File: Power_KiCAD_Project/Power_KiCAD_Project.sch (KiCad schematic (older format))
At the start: 5 parts

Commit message: Changed labels from global to local
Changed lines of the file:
@@
 Text Notes 1750 2900 2    100  ~ 0
 SWD Connector
-Text GLabel 1300 1500 2    50   Input ~ 0
-I2C1_SDA
-Text GLabel 1300 1600 2    50   Input ~ 0
-I2C1_SCL
 Text Notes 600  2400 0    50   ~ 0
 Current version uses connector data\nbus for communications to BMS.\nThis may not be ideal, and perhaps a \ndedicated communcation line\nto the BMS should be used instead.
@@
 Wire Bus Line
 	5600 1050 5600 2600
+Text Label 1300 1500 0    50   ~ 0
+I2C1_SDA
+Text Label 1300 1600 0    50   ~ 0
+I2C1_SCL
 $EndSCHEMATC

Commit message: Updated With c=Connections
Added connections for power and for card slots
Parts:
- added J?: Barrel_Jack, symbol Connector:Barrel_Jack
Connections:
- wire segments 75 -> 79
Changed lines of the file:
@@
 $Descr A4 11693 8268
 encoding utf-8
-Sheet 1 5
+Sheet 1 6
 Title "Power Supply PCB Schematic"
 Date "2021-10-05"
@@
 	2500 5450 2500 5300
 Wire Wire Line
-	2500 5300 3100 5300
+	2500 5300 2950 5300
 Wire Wire Line
 	1500 5550 2500 5550
@@
 	2500 5550 2500 6050
 Wire Wire Line
-	2500 6050 3100 6050
+	2500 6050 2750 6050
 Wire Wire Line
 	1400 3350 2150 3350
@@
 NoConn ~ 1300 1700
 NoConn ~ 1300 1800
+Text Label 1300 1500 0    50   ~ 0
+I2C1_SDA
+Text Label 1300 1600 0    50   ~ 0
+I2C1_SCL
+$Sheet
+S 8500 4550 2050 1400
+U 6183A598
+F0 "Pcie_Connection" 50
+F1 "Pcie_Connection.sch" 50
+$EndSheet
+$Comp
+L Connector:Barrel_Jack J?
+U 1 1 61850F95
+P 2850 4550
+F 0 "J?" V 2861 4738 50  0000 L CNN
+F 1 "Barrel_Jack" V 2952 4738 50  0000 L CNN
+F 2 "" H 2900 4510 50  0001 C CNN
+F 3 "~" H 2900 4510 50  0001 C CNN
+	1    2850 4550
+	0    1    1    0
+$EndComp
+Wire Wire Line
+	2950 4850 2950 5300
+Connection ~ 2950 5300
+Wire Wire Line
+	2950 5300 3100 5300
+Wire Wire Line
+	2750 4850 2750 6050
 Wire Bus Line
 	1350 6500 1350 6800
@@
 Wire Bus Line
 	5600 1050 5600 2600
-Text Label 1300 1500 0    50   ~ 0
-I2C1_SDA
-Text Label 1300 1600 0    50   ~ 0
-I2C1_SCL
+Connection ~ 2750 6050
+Wire Wire Line
+	2750 6050 3100 6050
 $EndSCHEMATC

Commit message: Changes to bus
bus was changed
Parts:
- removed C?: 100nF, symbol Device:C_Small
- removed J?: ARM 10 Pin, 2X5-RA, symbol SparkFun-Connectors:CONN_05X2RA
- removed J?: CONN_06X2SMD_FEMALE, 2X6_SMD, symbol SparkFun-Connectors:CONN_06X2SMD_FEMALE
- removed J?: CONN_03X2FEMALE, 2X3, symbol SparkFun-Connectors:CONN_03X2FEMALE
- added J1, J3, J4, J5: XT60, 1X02, symbol SparkFun-Connectors:CONN_02
- J2: renamed from J?; Field4 LiPo Pack Connector -> Pack 2
- gave numbers to parts that had none: 1
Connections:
- net labels added: Alert_active, Alert_scl, Alert_sda, NRST, SWCLK, SWDIO
- net labels removed: +5V, I2C1_SCL, I2C1_SDA
- wire segments 79 -> 32
- no-connect marks 11 -> 24
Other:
- note removed: "Current version uses connector data\nbus for communications to BMS.\nThis may not be ideal, and perhaps a \ndedicated communcation line\nto the BMS should be used instead."
- note removed: "Main System Bus"
- note removed: "NRST cap protects\nagainst parasitic resets."
- note removed: "SWD Connector"
- moved on the sheet: J2

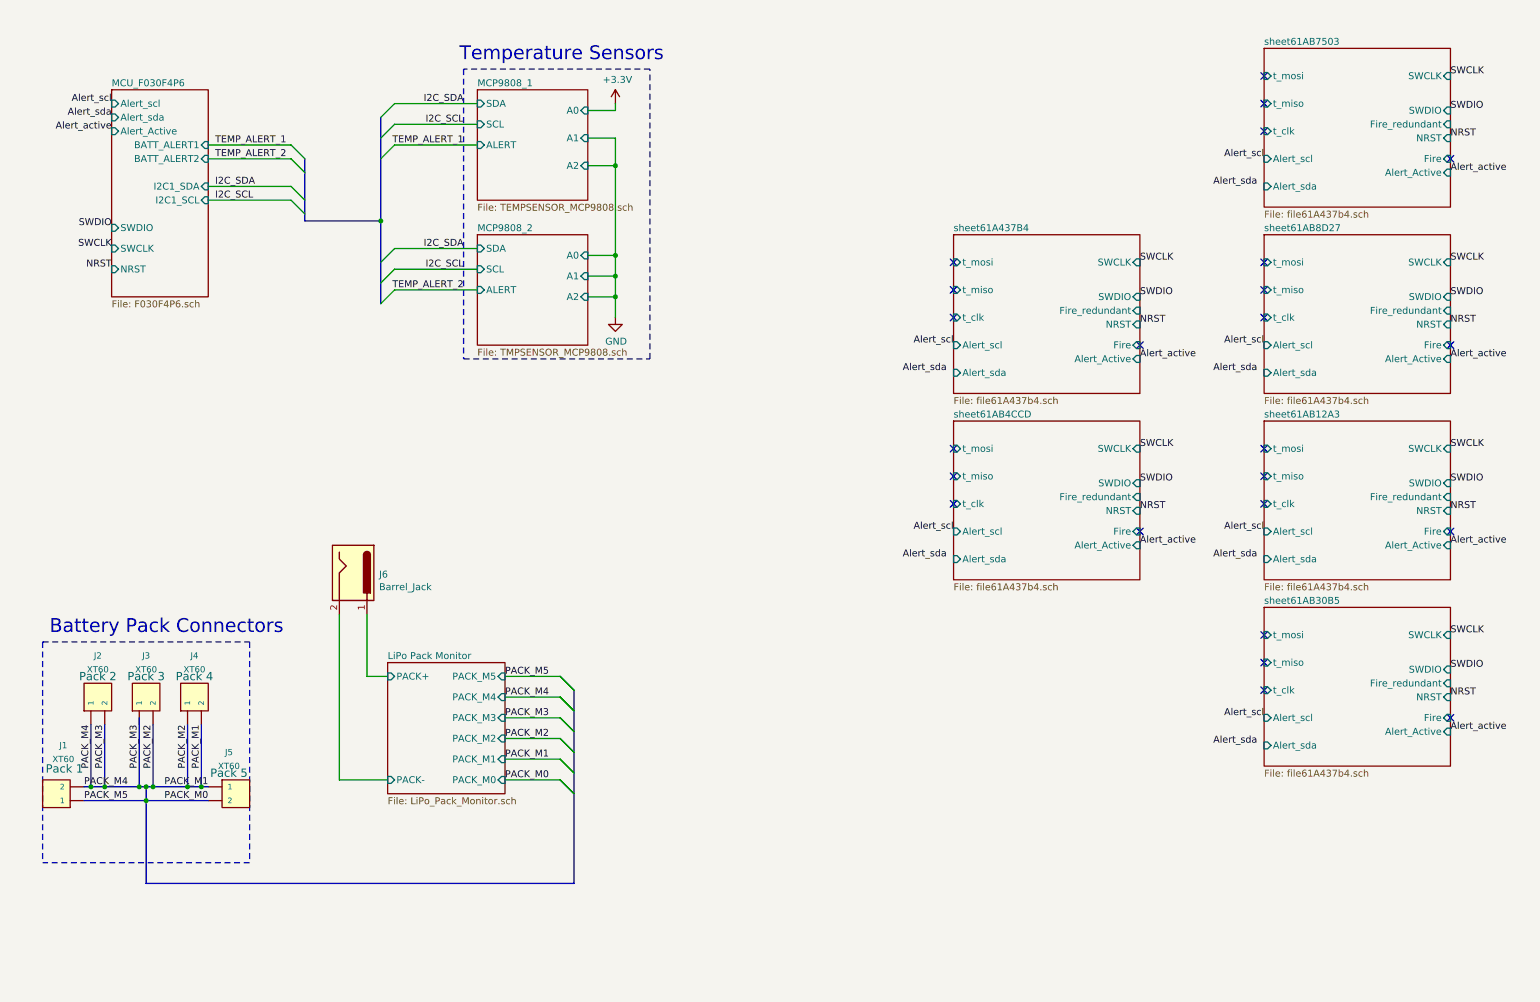
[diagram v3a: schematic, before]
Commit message: Added main Buck Converters & Question about grounding
I think that the BMS Ground needs to be separated from the main board ground since the BMS uses low side switching to protect the batteries. Like it is currently setup, the current can bypass the switches through ground.
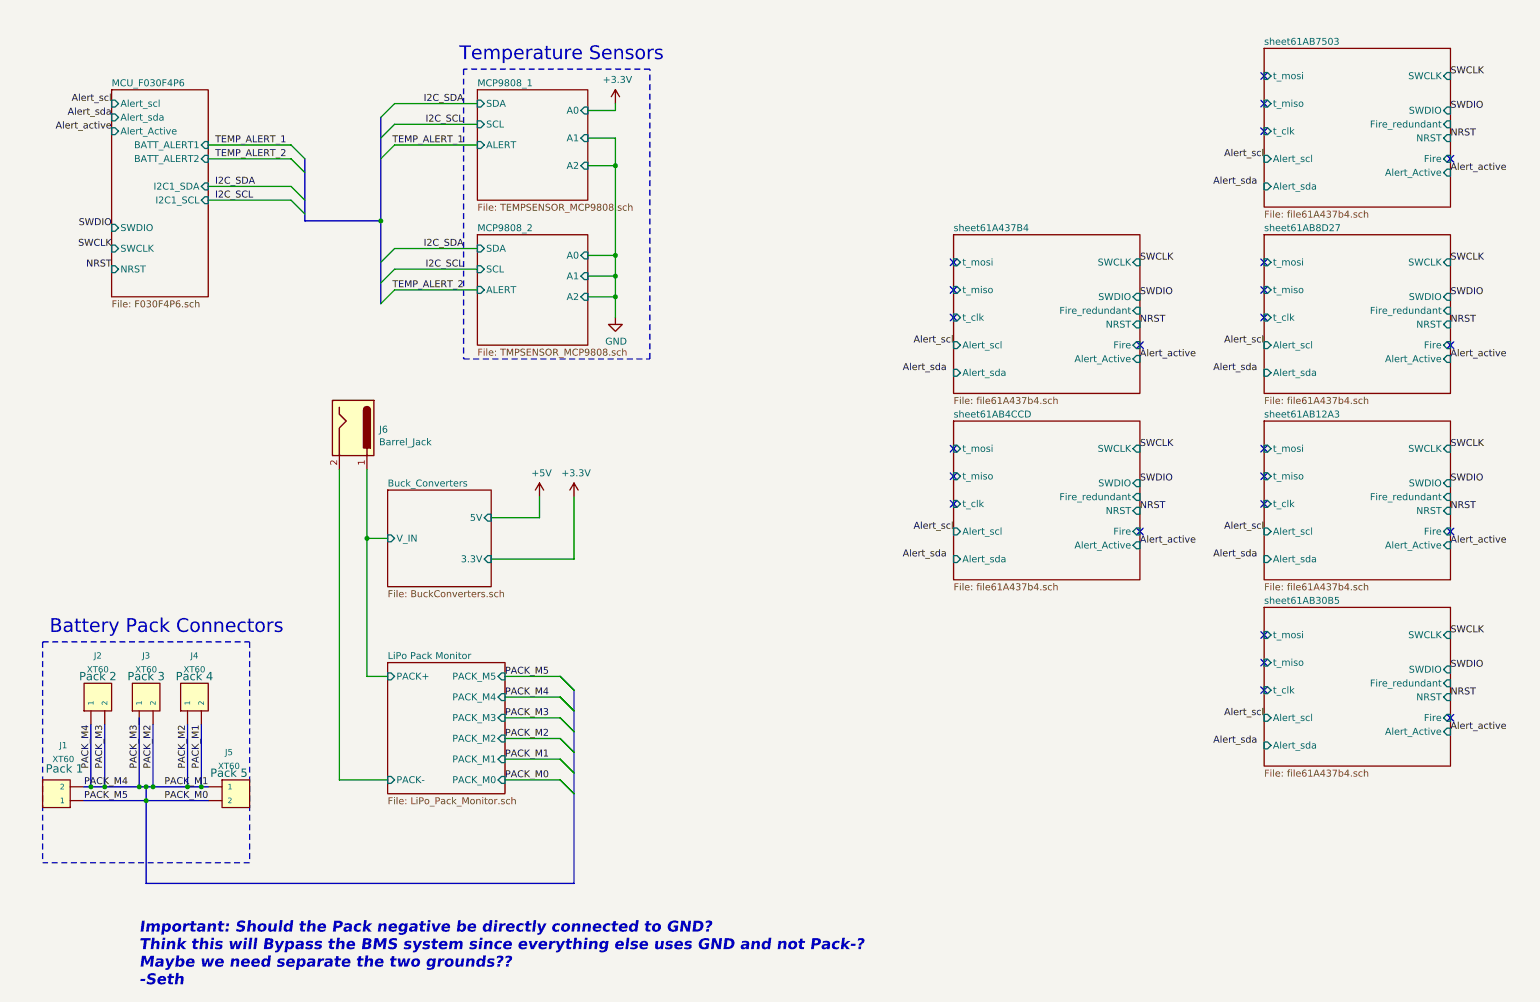
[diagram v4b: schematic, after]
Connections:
- net LiPo Pack Monitor/PACK+ renamed Buck_Converters/V_IN
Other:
- note added: "Important: Should the Pack negative be directly connected to GND?\nThink this will Bypass the BMS system since everything else uses GND and not Pack-?\nMaybe we need separate the two grounds??\n-Seth"
- moved on the sheet: J6
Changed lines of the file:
@@
 $Descr A4 11693 8268
 encoding utf-8
-Sheet 1 11
+Sheet 1 12
 Title "Power Supply PCB Schematic"
 Date "2021-10-05"
@@
 L Connector:Barrel_Jack J6
 U 1 1 61850F95
-P 2850 4550
-F 0 "J6" V 2861 4738 50  0000 L CNN
-F 1 "Barrel_Jack" V 2952 4738 50  0000 L CNN
-F 2 "" H 2900 4510 50  0001 C CNN
-F 3 "~" H 2900 4510 50  0001 C CNN
-	1    2850 4550
+P 2850 3500
+F 0 "J6" V 2861 3688 50  0000 L CNN
+F 1 "Barrel_Jack" V 2952 3688 50  0000 L CNN
+F 2 "" H 2900 3460 50  0001 C CNN
+F 3 "~" H 2900 3460 50  0001 C CNN
+	1    2850 3500
 	0    1    1    0
 $EndComp
 Wire Wire Line
-	2950 4850 2950 5300
-Wire Wire Line
 	2950 5300 3100 5300
-Wire Wire Line
-	2750 4850 2750 6050
 Wire Wire Line
 	2750 6050 3100 6050
@@
 Wire Bus Line
 	1050 5650 1050 6100
-Wire Bus Line
-	3050 2000 3050 2600
-Wire Bus Line
-	3050 1250 3050 2000
-Wire Bus Line
-	2500 1550 2500 2000
-Wire Bus Line
-	4450 5400 4450 6800
 Connection ~ 1050 6100
 Wire Bus Line
@@
 Text Label 1800 6200 2    50   ~ 0
 PACK_M0
+$Sheet
+S 3100 3950 750  700
+U 61A48488
+F0 "Buck_Converters" 50
+F1 "BuckConverters.sch" 50
+F2 "V_IN" I L 3100 4300 50
+F3 "3.3V" I R 3850 4450 50
+F4 "5V" I R 3850 4150 50
+$EndSheet
+Wire Wire Line
+	2750 3800 2750 6050
+Wire Wire Line
+	2950 3800 2950 4300
+Wire Wire Line
+	3100 4300 2950 4300
+Connection ~ 2950 4300
+Wire Wire Line
+	2950 4300 2950 5300
+$Comp
+L power:+3.3V #PWR?
+U 1 1 61A5452E
+P 4450 4000
+F 0 "#PWR?" H 4450 3850 50  0001 C CNN
+F 1 "+3.3V" H 4465 4173 50  0000 C CNN
+F 2 "" H 4450 4000 50  0001 C CNN
+F 3 "" H 4450 4000 50  0001 C CNN
+	1    4450 4000
+	1    0    0    -1
+$EndComp
+$Comp
+L power:+5V #PWR?
+U 1 1 61A56282
+P 4200 4000
+F 0 "#PWR?" H 4200 3850 50  0001 C CNN
+F 1 "+5V" H 4215 4173 50  0000 C CNN
+F 2 "" H 4200 4000 50  0001 C CNN
+F 3 "" H 4200 4000 50  0001 C CNN
+	1    4200 4000
+	1    0    0    -1
+$EndComp
+Wire Wire Line
+	3850 4150 4200 4150
+Wire Wire Line
+	4200 4150 4200 4000
+Wire Wire Line
+	4450 4000 4450 4450
+Wire Bus Line
+	3050 2000 3050 2600
+Wire Bus Line
+	3050 1250 3050 2000
+Wire Bus Line
+	2500 1550 2500 2000
+Wire Bus Line
+	4450 5400 4450 6800
+Wire Wire Line
+	4450 4450 3850 4450
+Text Notes 1300 7550 0    79   Italic 16
+Important: Should the Pack negative be directly connected to GND?\nThink this will Bypass the BMS system since everything else uses GND and not Pack-?\nMaybe we need separate the two grounds??\n-Seth
 $EndSCHEMATC

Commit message: added components
added a few components and the correct numbers
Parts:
- removed J1, J2, J3, J4, J5: XT60, 1X02, symbol SparkFun-Connectors:CONN_02
- added J1, J2, J3, J4, J5: XT60-M, XT60-M:AMASS_XT60-M, symbol XT60-M:XT60-M
- J6: footprint (none) -> Connector_BarrelJack:BarrelJack_CUI_PJ-036AH-SMT_Horizontal
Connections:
- net PACK_M0: now also J5.2 (+)
- net PACK_M1: now also J4.2 (+), J5.1 (-)
- net PACK_M2: now also J3.2 (+), J4.1 (-)
- net PACK_M3: now also J2.2 (+)
- net PACK_M4: now also J1.2 (+), J2.1 (-)
- net PACK_M5: now also J1.1 (-)
- net LiPo Pack Monitor/PACK- renamed Pack-
- no-connect marks 24 -> 0

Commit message: pcb finished
pcb is done. 3am kicad be like
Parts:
- removed J6: Barrel_Jack, Connector_BarrelJack:BarrelJack_CUI_PJ-036AH-SMT_Horizontal, symbol Connector:Barrel_Jack
- added J6: PJ-102AH, PJ-102AH, symbol SamacSys_Parts:PJ-102AH
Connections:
- net Buck_Converters/V_IN: now also J6.1
- net PACK_M3: now also J3.1 (-)
- net Pack-: now also J6.2
- no-connect marks 0 -> 1

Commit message: Changes to PCB
Bunch of changes to layout with components on the other side
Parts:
- J6: footprint PJ-102AH -> SamacSys_Parts:PJ-102AH
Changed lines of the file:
@@
 F 0 "J6" V 3154 2672 50  0000 R CNN
 F 1 "PJ-102AH" V 3245 2672 50  0000 R CNN
-F 2 "PJ-102AH" H 3450 3000 50  0001 L CNN
+F 2 "SamacSys_Parts:PJ-102AH" H 3450 3000 50  0001 L CNN
 F 3 "http://www.cui.com/product/resource/digikeypdf/pj-102ah.pdf" H 3450 2900 50  0001 L CNN
 F 4 "DC POWER JACK" H 3450 2800 50  0001 L CNN "Description"
@@
 	2750 3700 2750 6050
 NoConn ~ 2800 2900
-Wire Bus Line
-	3050 2000 3050 2600
-Wire Bus Line
-	3050 1250 3050 2000
-Wire Bus Line
-	2500 1550 2500 2000
-Wire Bus Line
-	4450 5400 4450 6800
 $Sheet
 S 3100 5200 850  950
@@
 F9 "PACK-" I L 3100 6050 50
 $EndSheet
+Wire Bus Line
+	3050 2000 3050 2600
+Wire Bus Line
+	3050 1250 3050 2000
+Wire Bus Line
+	2500 1550 2500 2000
+Wire Bus Line
+	4450 5400 4450 6800
 $EndSCHEMATC
